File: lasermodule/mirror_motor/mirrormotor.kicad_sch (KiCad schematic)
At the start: 45 parts, among them IC1 NBC3111, J1 R, J10 292173-5, J2 R, J3 R, J4 R, J5 R, J6 R, J7 R, J8 R, J9 R

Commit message: board almost fully synced close for release
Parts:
- renumbered C11 to C1, C3 to C10, C14 to C11, C15 to C12, C12 to C13, C4 to C14, C7 to C15, C1 to C3, C10 to C4, C9 to C5, C8 to C6, C6 to C7, C5 to C8, C13 to C9, J3 to J1, J4 to J2, J9 to J3, J8 to J4, J6 to J5, J2 to J6, J1 to J7, J5 to J8, J7 to J9, R6 to R1, R9 to R10, R2 to R11, R1 to R13, R3 to R14, R11 to R15, R7 to R2, R13 to R3, R10 to R4, R8 to R5, R5 to R6, R4 to R7, R15 to R8, R14 to R9
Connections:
- net PWM: now reaches J10.1
- net GND: now reaches J10.3
- net GND: now also J10.4
- net +12V: now reaches J10.5
- no-connect marks 0 -> 1
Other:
- moved on the sheet: C1, C13, R9

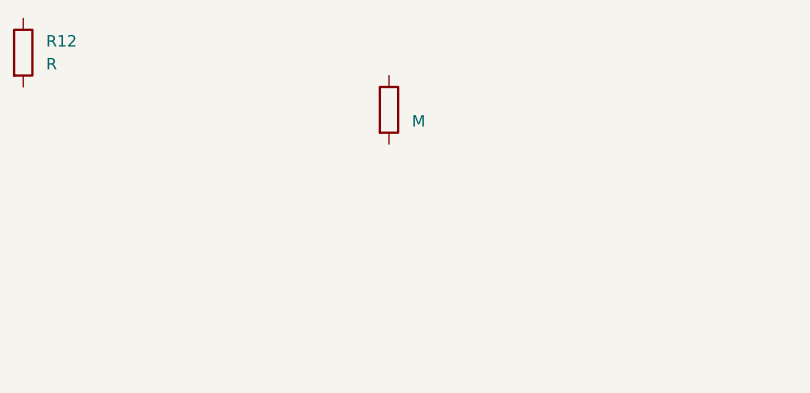
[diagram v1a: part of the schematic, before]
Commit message: added new driver for pcb motor
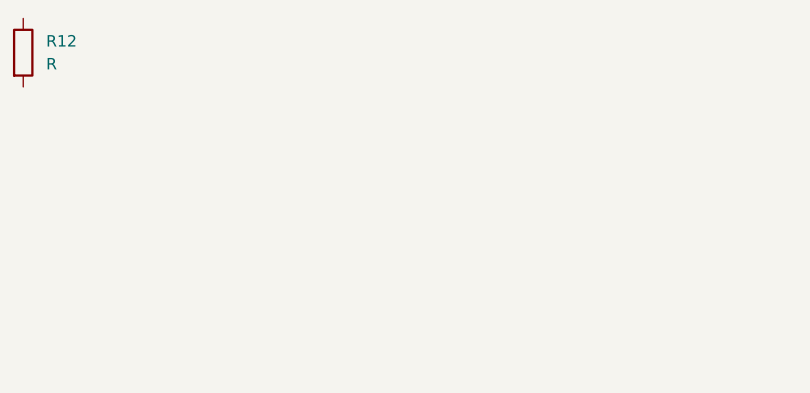
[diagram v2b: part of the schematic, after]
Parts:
- removed R16: M, mirrormotor:motor, symbol Device:R
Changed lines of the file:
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@@
-	)
-	(symbol
-		(lib_id "Device:R")
-		(at 110.49 31.75 0)
-		(unit 1)
-		(exclude_from_sim no)
-		(in_bom yes)
-		(on_board yes)
-		(dnp no)
-		(fields_autoplaced yes)
-		(property "Reference" "R16"
-			(at 113.03 30.4799 0)
-			(effects
-				(font
-					(size 1.27 1.27)
-				)
-				(justify left)
-				(hide yes)
-			)
-		)
-		(property "Value" "M"
-			(at 113.03 33.0199 0)
-			(effects
-				(font
-					(size 1.27 1.27)
-				)
-				(justify left)
-			)
-		)
-		(property "Footprint" "mirrormotor:motor"
-			(at 108.712 31.75 90)
-			(effects
-				(font
-					(size 1.27 1.27)
-				)
-				(hide yes)
-			)
-		)
-		(property "Datasheet" "~"
-			(at 110.49 31.75 0)
-			(effects
-				(font
-					(size 1.27 1.27)
-				)
-				(hide yes)
-			)
-		)
-		(property "Description" "Resistor"
-			(at 110.49 31.75 0)
-			(effects
-				(font
-					(size 1.27 1.27)
-				)
-				(hide yes)
-			)
-		)
-		(pin "1"
-		)
-		(pin "2"
-		)
-		(instances
-			(project ""
-				(path "/02aeda72-ca3b-4b43-8ba2-cb54433722d4"
-					(reference "R16")
-					(unit 1)
-				)
-			)
-		)
 	)
 	(symbol
